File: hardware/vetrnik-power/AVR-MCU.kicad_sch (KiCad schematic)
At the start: 41 parts, among them J14 AC frequency sense, J15 AVR-ISP-6, J16 ACS712_2, J17 ACS712, Q10 BC846, Q9 BC847, SW1 AVR RESET, U10 LTV-817, U11 L78L05_TO92, U12 ATmega8-16PU, Y1 16MHz

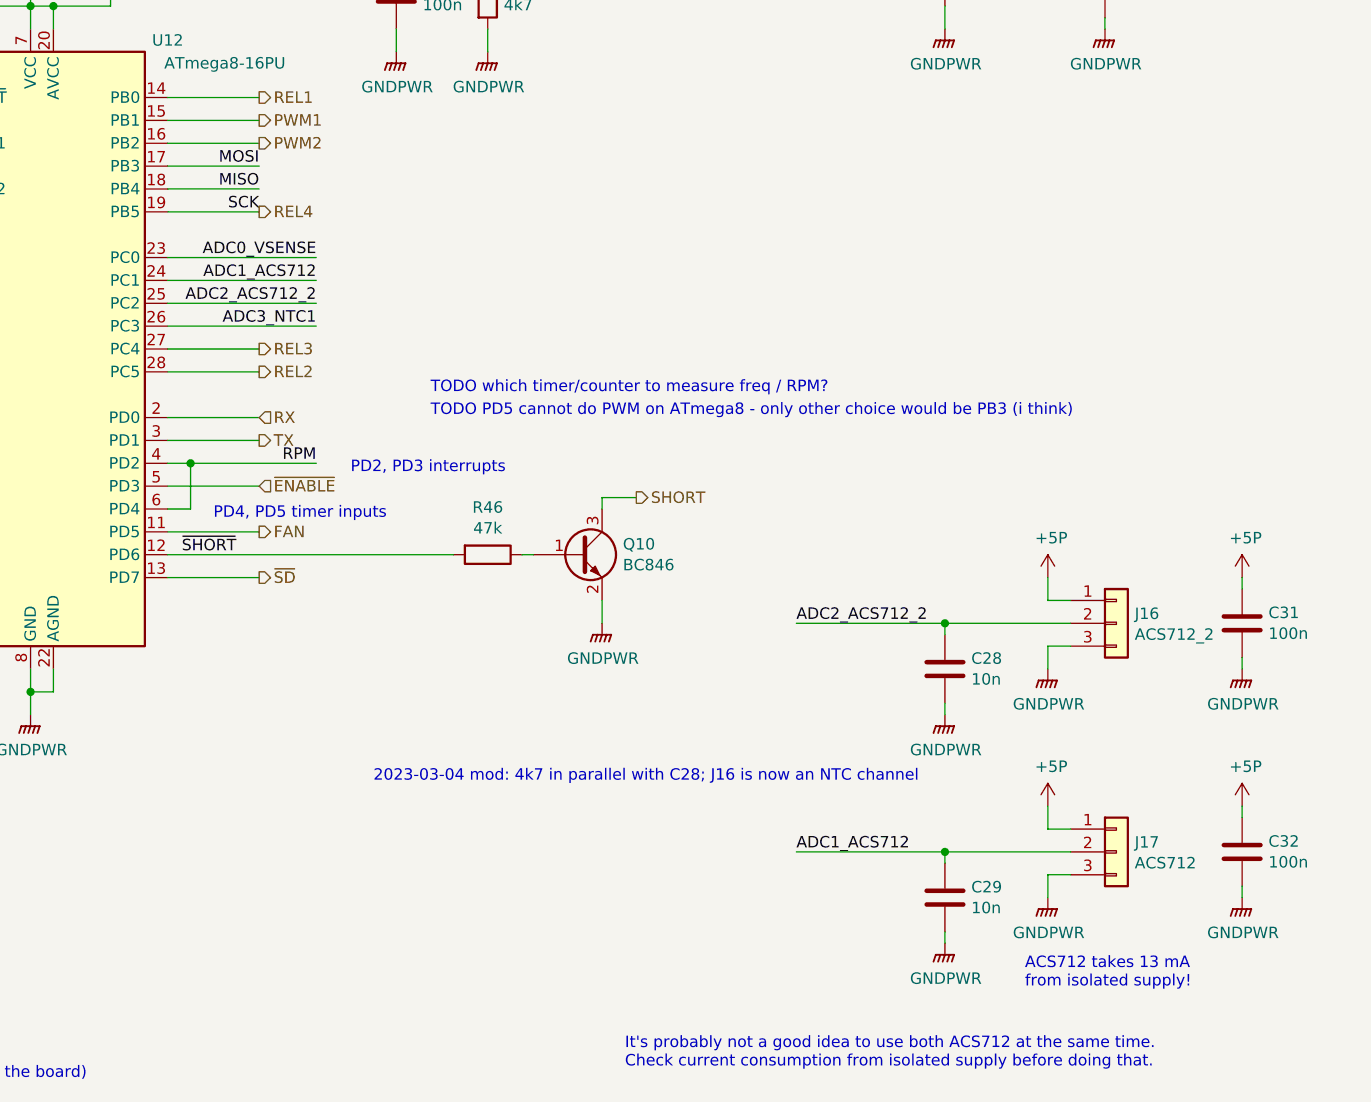
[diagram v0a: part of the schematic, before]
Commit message: [hardware] Add info about hardware mods
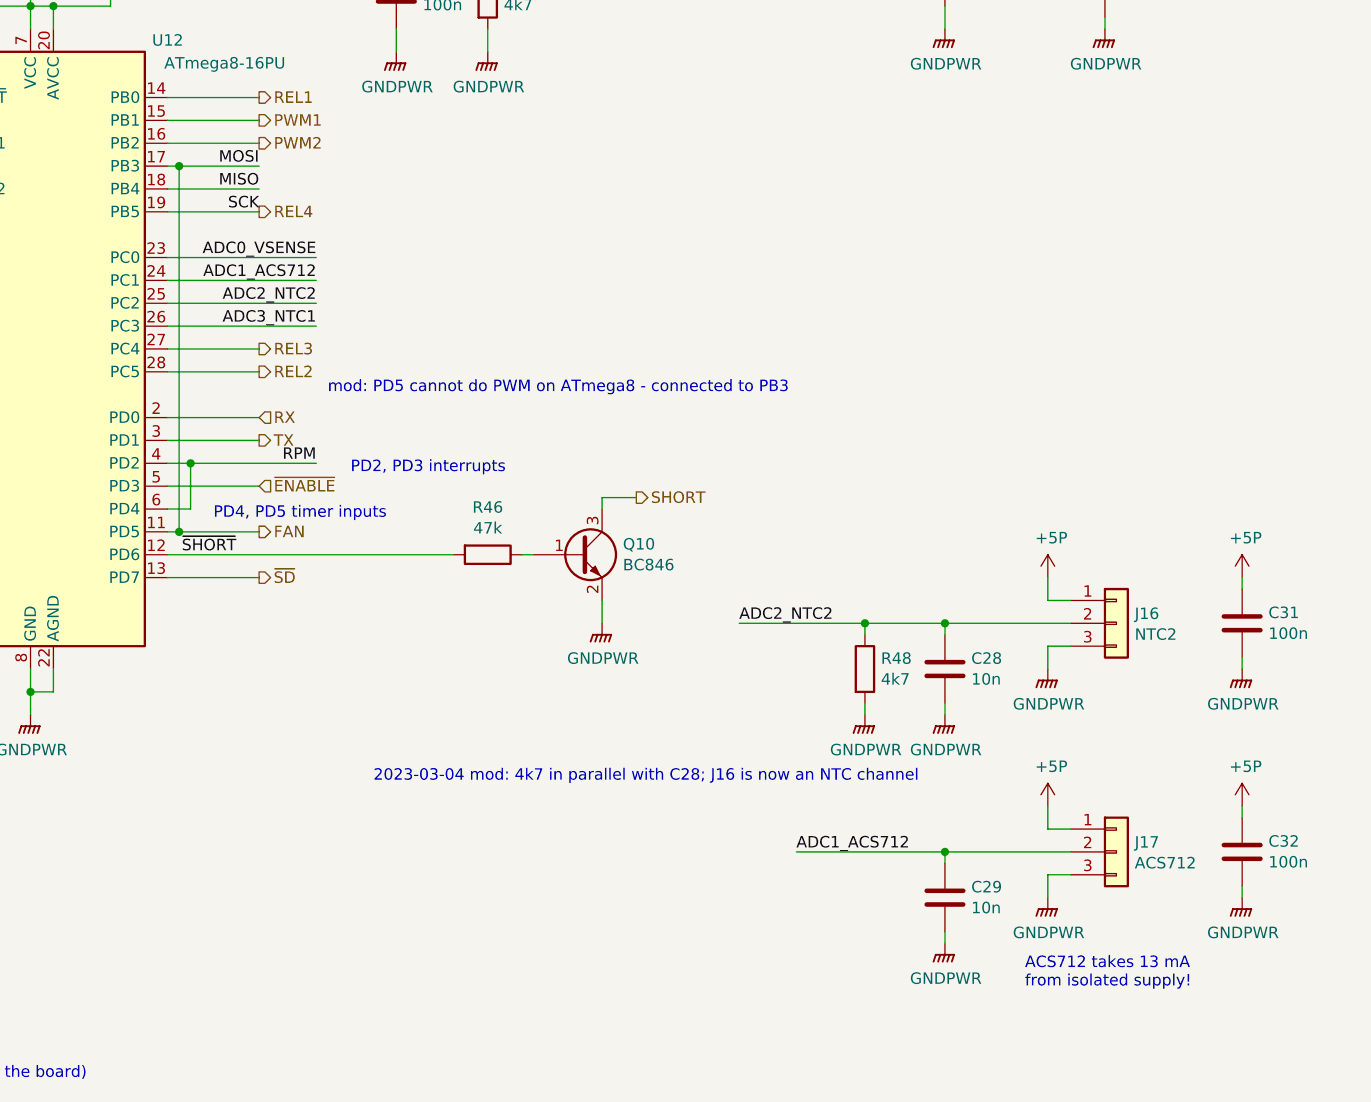
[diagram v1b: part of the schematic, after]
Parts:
- added R48: 4k7, Resistor_SMD:R_1206_3216Metric_Pad1.30x1.75mm_HandSolder, symbol Device:R
- J16: value ACS712_2 -> NTC2
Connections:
- net MOSI is gone; now on net FAN: J15.4 (MOSI), U12.17 (PB3)
- net GNDPWR: now also R48.2
- net ADC2_ACS712_2 renamed ADC2_NTC2
- net ADC2_NTC2: now also R48.1
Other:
- note added: "mod: PD5 cannot do PWM on ATmega8 - connected to PB3"
- note removed: "It's probably not a good idea to use both ACS712 at the same time. Check current consumption from isolated supply before doing that."
- note removed: "TODO PD5 cannot do PWM on ATmega8 - only other choice would be PB3 (i think)"
- note removed: "TODO which timer/counter to measure freq / RPM?"

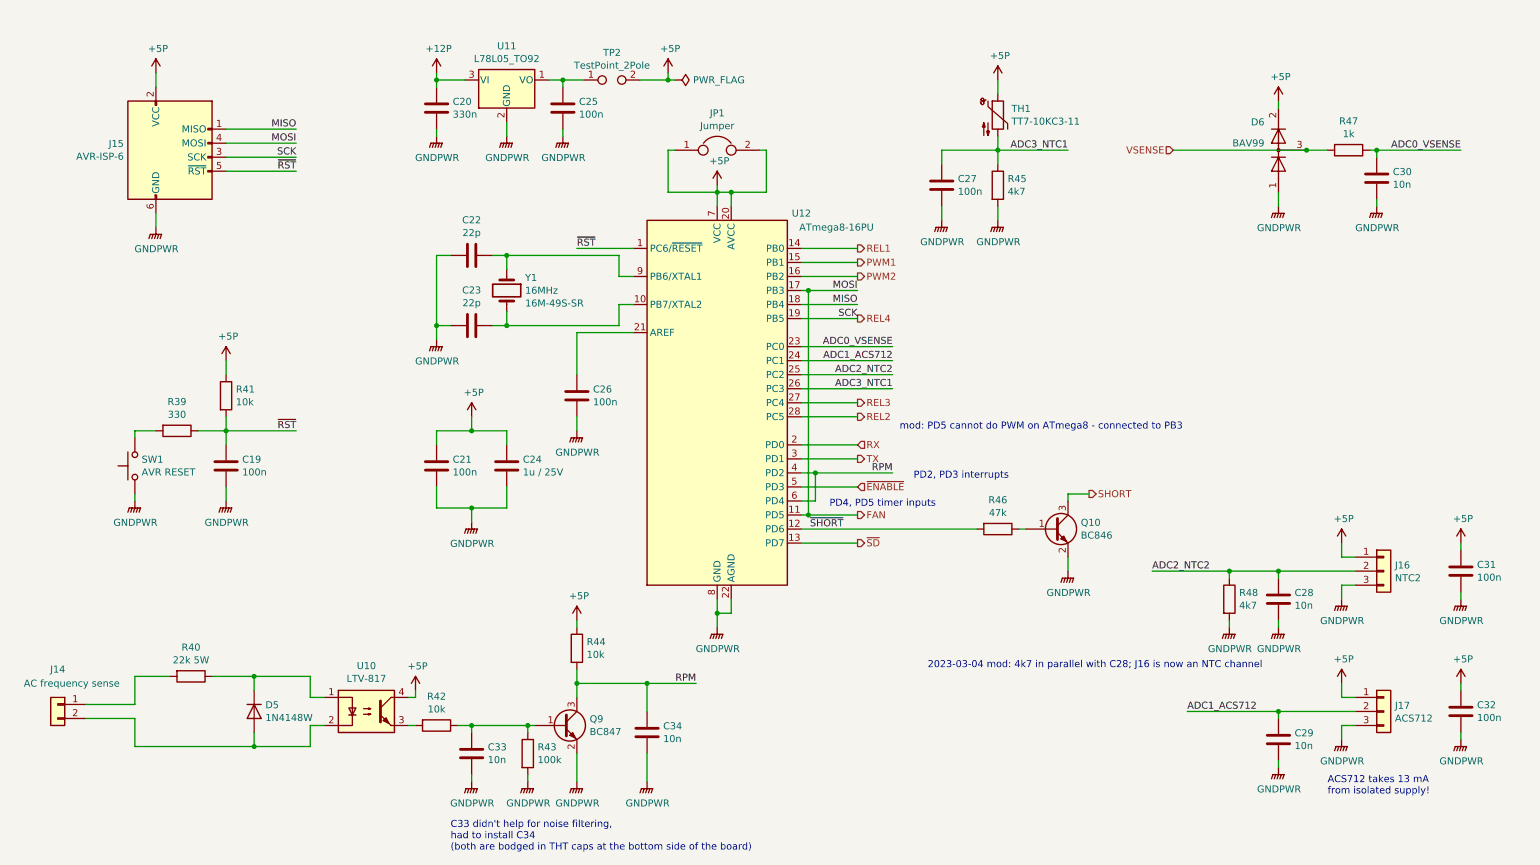
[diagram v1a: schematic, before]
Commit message: [hardware] Clean up vetrnik-power schematic
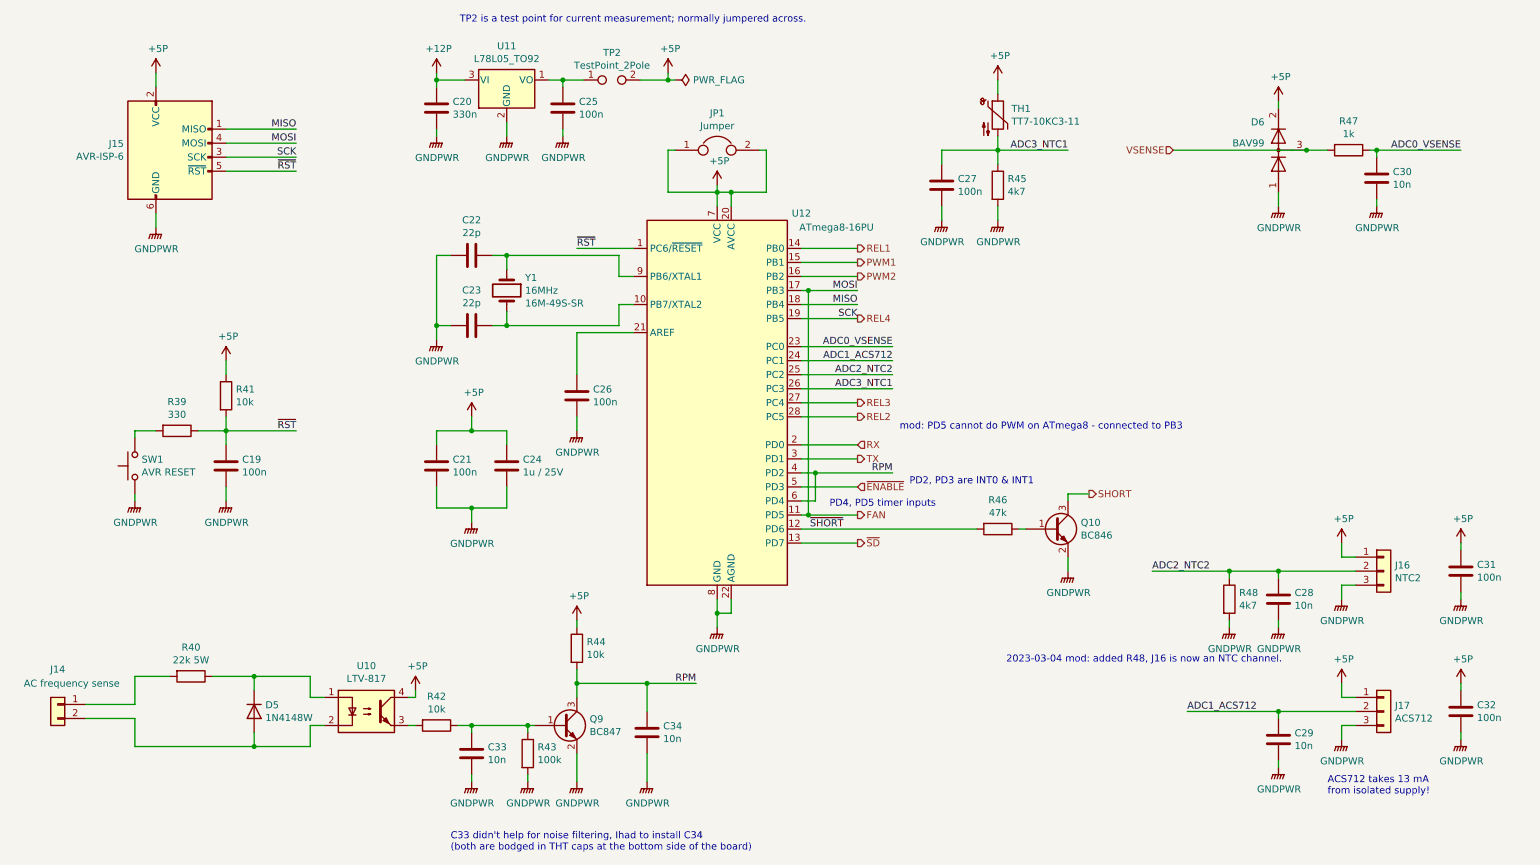
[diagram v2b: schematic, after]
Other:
- note added: "2023-03-04 mod: added R48, J16 is now an NTC channel."
- note added: "C33 didn't help for noise filtering, Ihad to install C34 (both are bodged in THT caps at the bottom side of the board)"
- note added: "PD2, PD3 are INT0 & INT1"
- note added: "TP2 is a test point for current measurement; normally jumpered across."
- note removed: "2023-03-04 mod: 4k7 in parallel with C28; J16 is now an NTC channel"
- note removed: "C33 didn't help for noise filtering, had to install C34 (both are bodged in THT caps at the bottom side of the board)"
- note removed: "PD2, PD3 interrupts"
- company: (none) -> Ondřej Sluka
- title: (none) -> vetrnik-power MCU
